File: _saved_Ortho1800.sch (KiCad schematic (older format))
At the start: 304 parts

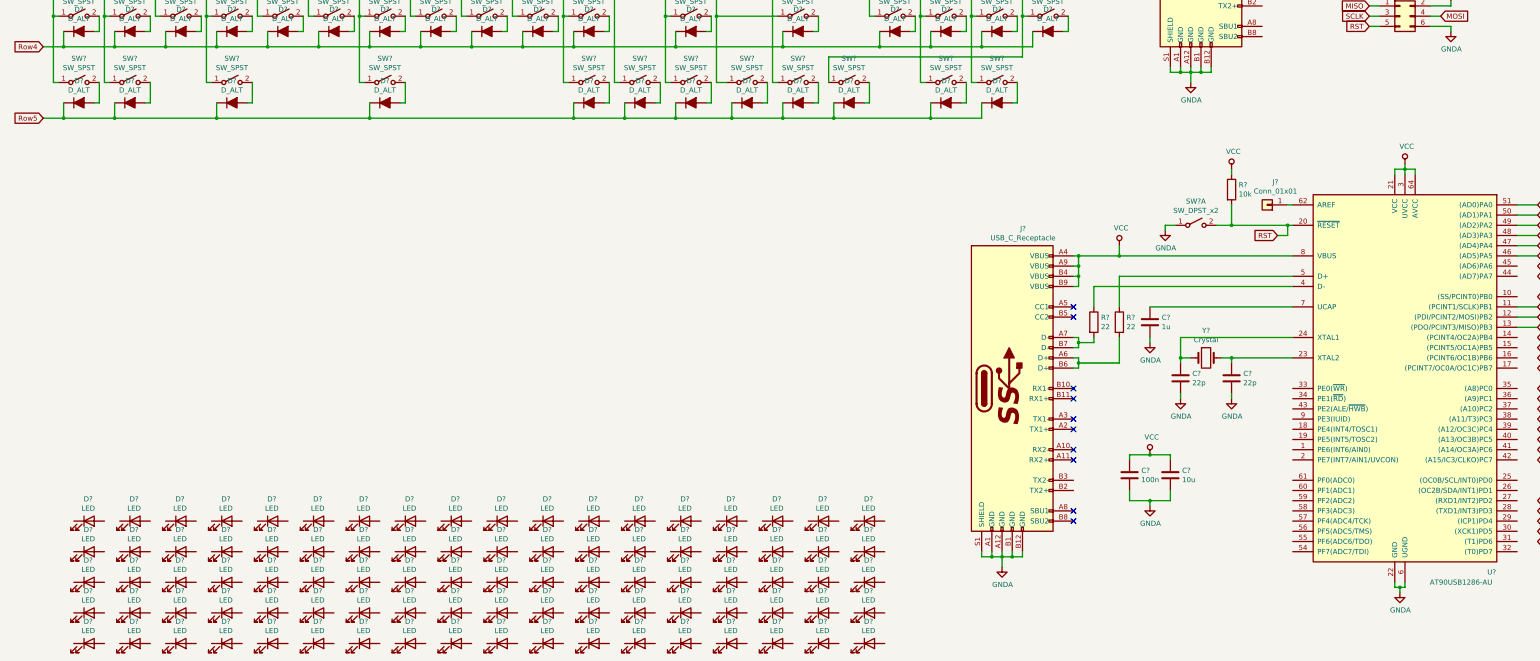
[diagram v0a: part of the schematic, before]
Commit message: Adding led matrix
Add led matrix and BT connector will see to add HC05 module later...
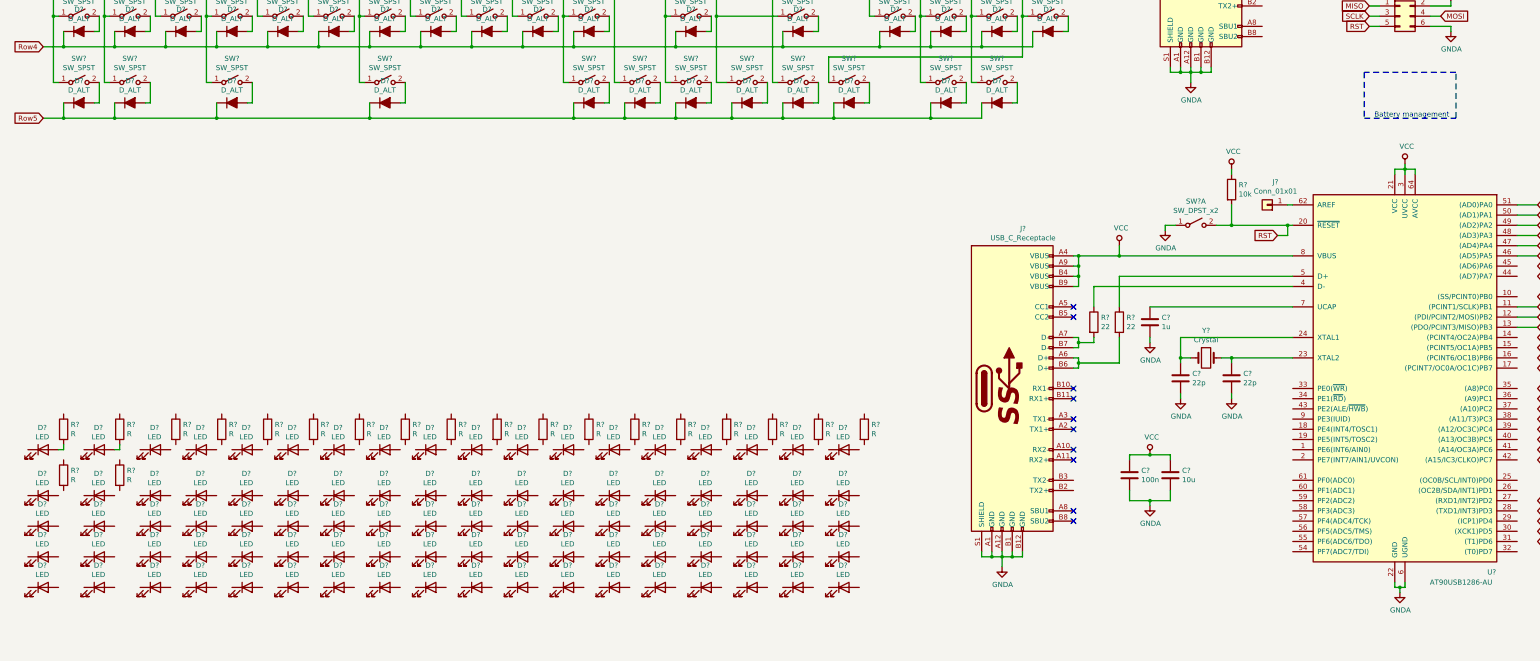
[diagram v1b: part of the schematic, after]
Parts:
- added R? (x20): R, symbol Device:R
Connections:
- net at D?.2 (A): now also R?.2 (x2)
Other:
- note added: "Battery management"
- moved on the sheet: D?
